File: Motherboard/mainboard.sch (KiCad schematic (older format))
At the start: 53 parts, among them IC1 BMX160, J1 Conn_01x01, J2 10118194-0001LF, J28 Conn_01x01, J29 Conn_01x01, J3 Micro_SD_Card, J30 Conn_01x01, J4 xf2m-2415-1a, J5 XF2M-1015-1A, J6 U.FL-R-SMT-1, J7 U.FL-R-SMT-1, J8 Conn_01x01, SW1 KMR231NG LFS, U1 RFM95W-915S2, U2 ATSAMD51G_TQFN48, U3 DRV8848, U4 TPS82740BSIPR, U5 DRV8848, U6 MAX708RESA-T, U8 RFM95W-915S2

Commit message: lots of clean up
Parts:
- removed D1: GREEN, LED_SMD:LED_0603_1608Metric, symbol mainboard-rescue:LED0805_NOOUTLINE-
- removed R1: 330, Resistor_SMD:R_0402_1005Metric, symbol mainboard-rescue:R_US-Device
- added D3: WS2812B, LED_SMD:LED_WS2812B_PLCC4_5.0x5.0mm_P3.2mm, symbol LED:WS2812B
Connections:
- net labels removed: CS_IMU
- wire segments 148 -> 147
- no-connect marks 10 -> 11
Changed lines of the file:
@@
-$EndComp
-$Comp
-L mainboard-rescue:R_US-Device R1
-U 1 1 5C3B885A
-P -250 6000
-F 0 "R1" H -350 5950 50  0000 C CNN
-F 1 "330" H -400 6050 50  0000 C CNN
-F 2 "Resistor_SMD:R_0402_1005Metric" V -210 5990 50  0001 C CNN
-F 3 "~" H -250 6000 50  0001 C CNN
-	1    -250 6000
-	-1   0    0    1
-$EndComp
-$Comp
-L mainboard-rescue:LED0805_NOOUTLINE- D?
-U 1 1 5C3B8860
-P -450 6150
-AR Path="/5BCFDB7D/5C3B8860" Ref="D?"  Part="1"
-AR Path="/5C3B8860" Ref="D1"  Part="1"
-F 0 "D1" H -500 6050 42  0000 C CNN
-F 1 "GREEN" H -600 6350 42  0001 C CNN
-F 2 "LED_SMD:LED_0603_1608Metric" H -450 6150 50  0001 C CNN
-F 3 "" H -450 6150 50  0001 C CNN
-	1    -450 6150
-	-1   0    0    1
 $EndComp
 $Comp
@@
 L power:GND #PWR0121
 U 1 1 5DB132FE
-P -600 6150
-F 0 "#PWR0121" H -600 5900 50  0001 C CNN
-F 1 "GND" H -595 5977 50  0000 C CNN
-F 2 "" H -600 6150 50  0001 C CNN
-F 3 "" H -600 6150 50  0001 C CNN
-	1    -600 6150
-	1    0    0    -1
-$EndComp
-Wire Wire Line
-	-600 6150 -550 6150
+P 650 6300
+F 0 "#PWR0121" H 650 6050 50  0001 C CNN
+F 1 "GND" H 655 6127 50  0000 C CNN
+F 2 "" H 650 6300 50  0001 C CNN
+F 3 "" H 650 6300 50  0001 C CNN
+	1    650  6300
+	1    0    0    -1
+$EndComp
 $Comp
 L power:GND #PWR0122
@@
 	1    0    0    -1
 $EndComp
-Text GLabel 2600 1600 2    59   Output ~ 0
-MOSI
-Text GLabel 2600 1500 2    59   Output ~ 0
-SCK
-Wire Wire Line
-	2600 1600 2500 1600
-Wire Wire Line
-	2600 1500 2500 1500
-Text GLabel 1200 1000 0    59   Input ~ 0
-MISO
-Wire Wire Line
-	1200 1000 1300 1000
-Wire Wire Line
-	2500 1400 2600 1400
-Text GLabel 2600 1400 2    50   Input ~ 0
-CS_IMU
 $Comp
 L power:GND #PWR0104
@@
 L power:+3V3 #PWR0105
 U 1 1 5DB0AC45
-P 2500 850
-F 0 "#PWR0105" H 2500 700 50  0001 C CNN
-F 1 "+3V3" H 2515 1023 50  0000 C CNN
-F 2 "" H 2500 850 50  0001 C CNN
-F 3 "" H 2500 850 50  0001 C CNN
-	1    2500 850
-	1    0    0    -1
-$EndComp
-Wire Wire Line
-	2500 850  2500 1000
+P 2600 850
+F 0 "#PWR0105" H 2600 700 50  0001 C CNN
+F 1 "+3V3" H 2615 1023 50  0000 C CNN
+F 2 "" H 2600 850 50  0001 C CNN
+F 3 "" H 2600 850 50  0001 C CNN
+	1    2600 850
+	1    0    0    -1
+$EndComp
+Wire Wire Line
+	2600 850  2600 1000
 $Comp
 L power:+3V3 #PWR0106
@@
 $EndComp
 Wire Wire Line
-	2700 1000 2500 1000
-Connection ~ 2500 1000
+	2700 1000 2600 1000
 $Comp
 L power:GND #PWR02
@@
 Wire Wire Line
 	8950 5750 8850 5750
-Text GLabel -1100 4850 2    50   Output ~ 0
-CS_IMU
 $Comp
 L power:GND #PWR0129
@@
 	1    0    0    -1
 $EndComp
+Text GLabel 2500 1600 2    59   BiDi ~ 0
+SDA1
+Text GLabel 2500 1500 2    59   BiDi ~ 0
+SCL1
+Wire Wire Line
+	2500 1400 2600 1400
+Wire Wire Line
+	2600 1400 2600 1000
+Connection ~ 2600 1000
+Wire Wire Line
+	2600 1000 2500 1000
+NoConn ~ 1300 1000
+$Comp
+L LED:WS2812B D3
+U 1 1 5DD8FF29
+P 650 6000
+F 0 "D3" H 306 6046 50  0000 R CNN
+F 1 "WS2812B" H 850 6400 50  0000 R CNN
+F 2 "LED_SMD:LED_WS2812B_PLCC4_5.0x5.0mm_P3.2mm" H 700 5700 50  0001 L TNN
+F 3 "https://cdn-shop.adafruit.com/datasheets/WS2812B.pdf" H 750 5625 50  0001 L TNN
+	1    650  6000
+	-1   0    0    -1
+$EndComp
+Wire Wire Line
+	950  6000 1450 6000
+$Comp
+L power:+3V3 #PWR0138
+U 1 1 5DDA79DB
+P 650 5700
+F 0 "#PWR0138" H 650 5550 50  0001 C CNN
+F 1 "+3V3" H 665 5873 50  0000 C CNN
+F 2 "" H 650 5700 50  0001 C CNN
+F 3 "" H 650 5700 50  0001 C CNN
+	1    650  5700
+	1    0    0    -1
+$EndComp

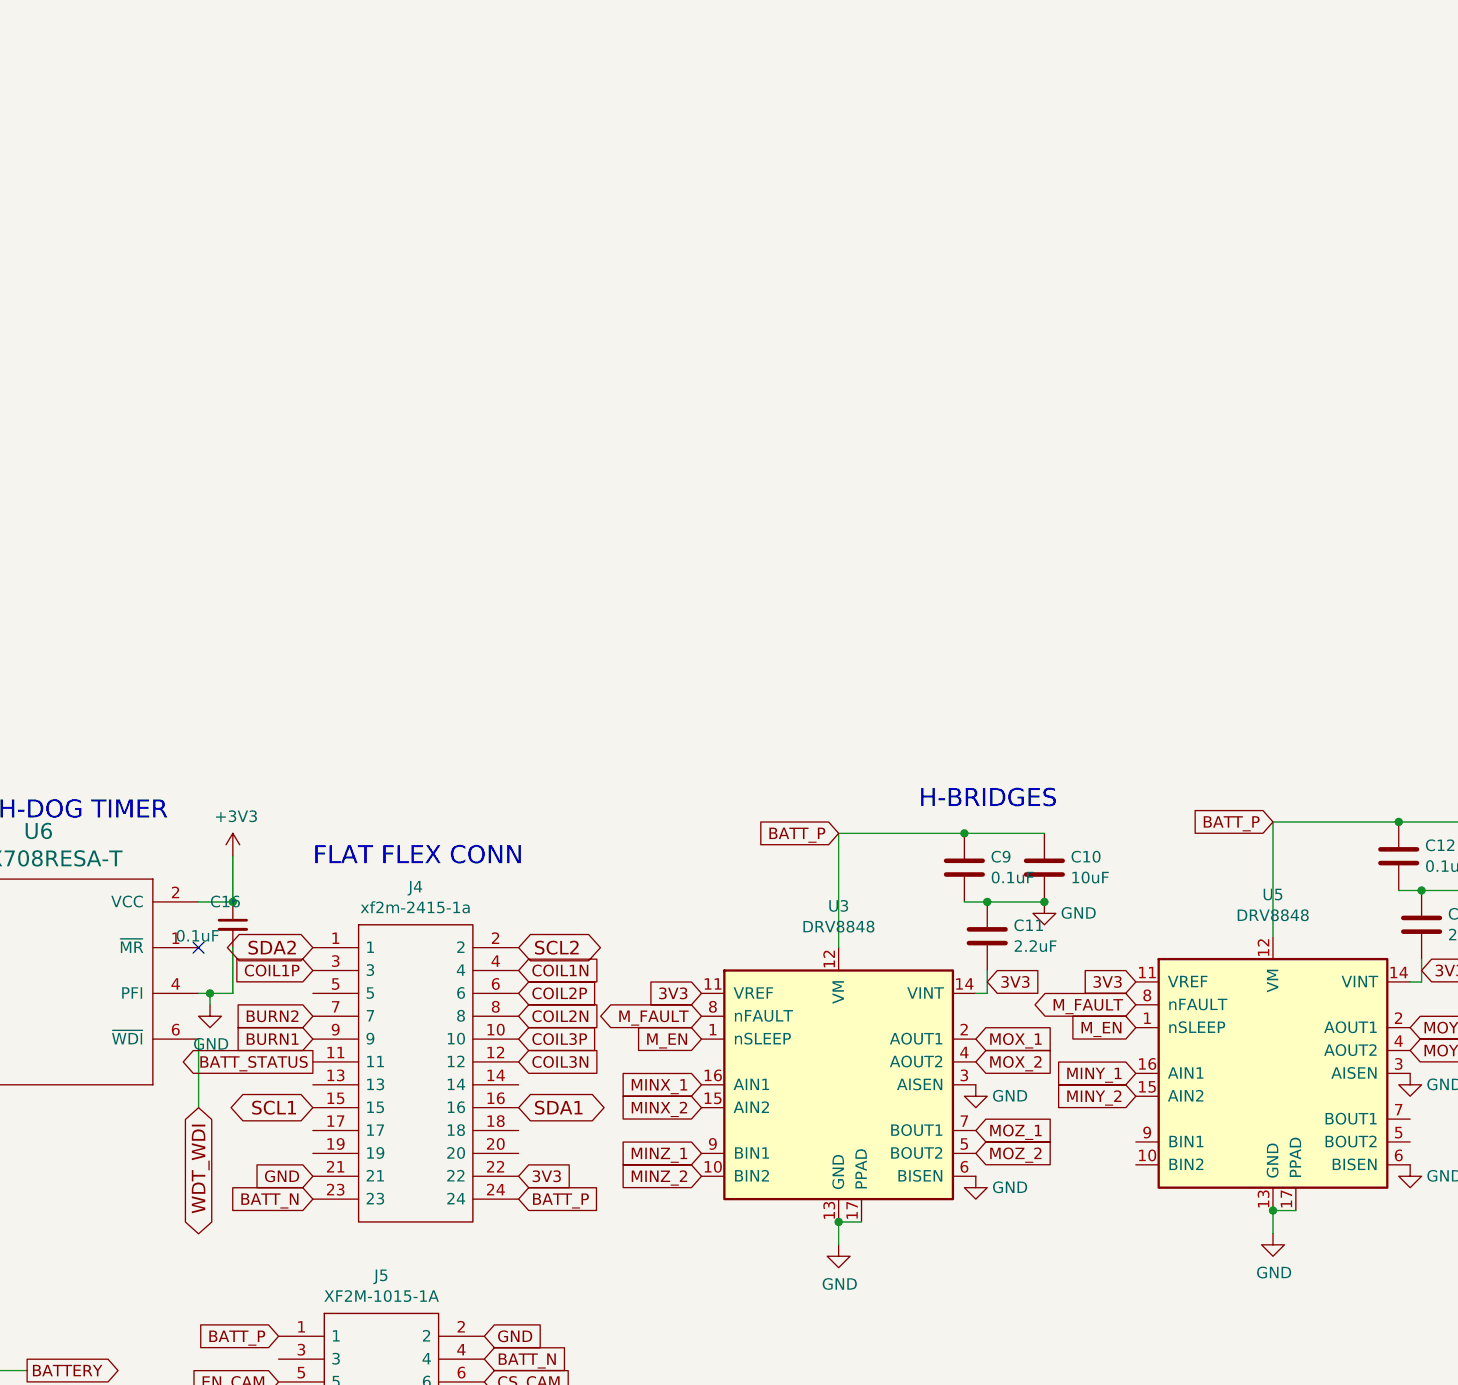
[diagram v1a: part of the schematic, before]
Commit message: putting matching coils in series
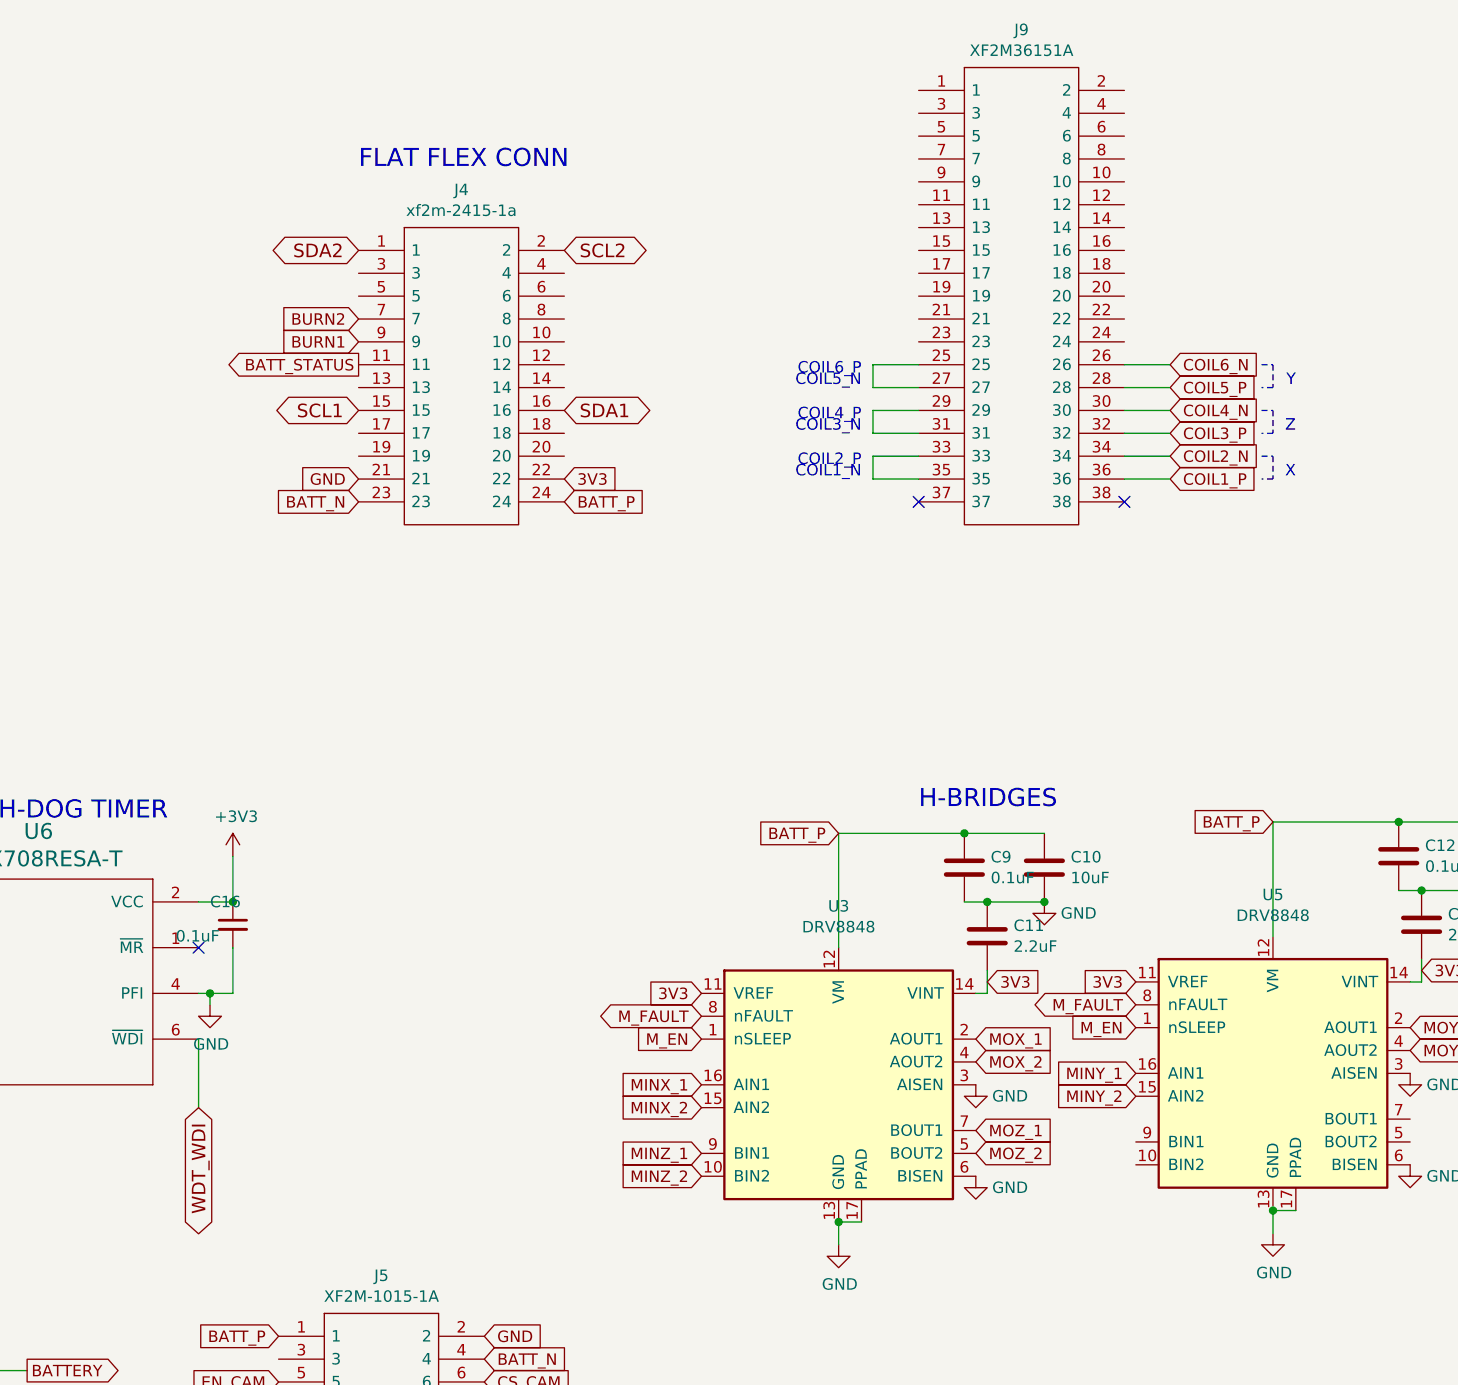
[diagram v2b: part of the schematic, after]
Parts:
- added J9: XF2M36151A, custom-footprints:XF2M36151A, symbol symbols:XF2M36151A
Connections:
- net COIL1N: no longer names the net of J4.4
- net COIL1P: no longer names the net of J4.3
- net COIL2N: no longer names the net of J4.8
- net COIL2P: no longer names the net of J4.6
- net COIL3N: no longer names the net of J4.12
- net COIL3P: no longer names the net of J4.10
- new net: J9.25, J9.27
- new net: J9.29, J9.31
- new net: J9.33, J9.35
- new net COIL1_P: J9.36
- new net COIL2_N: J9.34
- new net COIL3_P: J9.32
- new net COIL4_N: J9.30
- new net COIL5_P: J9.28
- new net COIL6_N: J9.26
- no-connect marks 11 -> 13
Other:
- note added: "COIL1_N"
- note added: "COIL2_P"
- note added: "COIL3_N"
- note added: "COIL4_P"
- note added: "COIL5_N"
- note added: "COIL6_P"
- note added: "X"
- note added: "Y"
- note added: "Z"
- moved on the sheet: J4
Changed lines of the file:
@@
 L mainboard-rescue:xf2m-2415-1a-symbols J4
 U 1 1 5DBA91E1
-P 5200 1250
-F 0 "J4" H 5650 1515 50  0000 C CNN
-F 1 "xf2m-2415-1a" H 5650 1424 50  0000 C CNN
-F 2 "custom-footprints:XF2M-2415-1A" H 5950 1350 50  0001 L CNN
-F 3 "http://docs-emea.rs-online.com/webdocs/0fd2/0900766b80fd28a0.pdf" H 5950 1250 50  0001 L CNN
-F 4 "Omron XF2M Series 0.5mm Pitch 24 Way 1 Row Right Angle SMT Female FPC Connector Locking Mechanism, Gold Plated Contacts" H 5950 1150 50  0001 L CNN "Description"
-	1    5200 1250
+P 5400 -1800
+F 0 "J4" H 5850 -1535 50  0000 C CNN
+F 1 "xf2m-2415-1a" H 5850 -1626 50  0000 C CNN
+F 2 "custom-footprints:XF2M-2415-1A" H 6150 -1700 50  0001 L CNN
+F 3 "http://docs-emea.rs-online.com/webdocs/0fd2/0900766b80fd28a0.pdf" H 6150 -1800 50  0001 L CNN
+F 4 "Omron XF2M Series 0.5mm Pitch 24 Way 1 Row Right Angle SMT Female FPC Connector Locking Mechanism, Gold Plated Contacts" H 6150 -1900 50  0001 L CNN "Description"
+	1    5400 -1800
 	1    0    0    -1
 $EndComp
@@
 Text Notes 1800 650  0    79   ~ 0
 IMU
-Text Notes 5200 900  0    79   ~ 0
+Text Notes 5400 -2150 0    79   ~ 0
 FLAT FLEX CONN
 $Comp
@@
 Text GLabel 5300 5800 2    59   BiDi ~ 0
 SCL2
-Text GLabel 6100 2250 2    50   Input ~ 0
+Text GLabel 6300 -800 2    50   Input ~ 0
 3V3
-Text GLabel 5200 2250 0    50   Input ~ 0
+Text GLabel 5400 -800 0    50   Input ~ 0
 GND
-Text GLabel 6100 2350 2    50   Input ~ 0
+Text GLabel 6300 -700 2    50   Input ~ 0
 BATT_P
-Text GLabel 5200 2350 0    50   Input ~ 0
+Text GLabel 5400 -700 0    50   Input ~ 0
 BATT_N
-Text GLabel 5200 1650 0    50   Input ~ 0
+Text GLabel 5400 -1400 0    50   Input ~ 0
 BURN1
-Text GLabel 5200 1550 0    50   Input ~ 0
+Text GLabel 5400 -1500 0    50   Input ~ 0
 BURN2
-Text GLabel 5200 1350 0    50   Input ~ 0
-COIL1P
-Text GLabel 6100 1350 2    50   Input ~ 0
-COIL1N
+Text GLabel 8950 -800 2    50   Input ~ 0
+COIL1_P
 Wire Wire Line
 	4750 1450 4700 1450
 Wire Wire Line
 	4750 1450 4750 1500
-Text GLabel 6100 1450 2    50   Input ~ 0
-COIL2P
-Text GLabel 6100 1550 2    50   Input ~ 0
-COIL2N
-Text GLabel 6100 1650 2    50   Input ~ 0
-COIL3P
-Text GLabel 6100 1750 2    50   Input ~ 0
-COIL3N
+Text GLabel 8950 -1000 2    50   Input ~ 0
+COIL3_P
 Text GLabel 5300 5900 2    59   BiDi ~ 0
 SDA2
@@
 Text Notes 2600 7900 0    50   ~ 0
 I2C_1\nSCL: PA01\nSDA: PA00\n\nI2C_2\nSCL: PA16\nSDA: PA17\n
-Text GLabel 6100 1950 2    59   BiDi ~ 0
+Text GLabel 6300 -1100 2    59   BiDi ~ 0
 SDA1
-Text GLabel 5200 1950 0    59   BiDi ~ 0
+Text GLabel 5400 -1100 0    59   BiDi ~ 0
 SCL1
-Text GLabel 6100 1250 2    59   BiDi ~ 0
+Text GLabel 6300 -1800 2    59   BiDi ~ 0
 SCL2
-Text GLabel 5200 1250 0    59   BiDi ~ 0
+Text GLabel 5400 -1800 0    59   BiDi ~ 0
 SDA2
 $Comp
@@
 Text GLabel 4450 6000 2    50   Input ~ 0
 BATT_STATUS
-Text GLabel 5200 1750 0    50   Output ~ 0
+Text GLabel 5400 -1300 0    50   Output ~ 0
 BATT_STATUS
 Text GLabel 4450 4700 2    50   BiDi ~ 0
@@
 	1    0    0    -1
 $EndComp
+$Comp
+L symbols:XF2M36151A J9
+U 1 1 5DB2822E
+P 7850 -2500
+F 0 "J9" H 8300 -2235 50  0000 C CNN
+F 1 "XF2M36151A" H 8300 -2326 50  0000 C CNN
+F 2 "custom-footprints:XF2M36151A" H 8600 -2400 50  0001 L CNN
+F 3 "http://static6.arrow.com/aropdfconversion/f8465b8f741f73dad8a8ab6be1baa1fc7c7bc980/19899915823643en-xf2m.pdf" H 8600 -2500 50  0001 L CNN
+F 4 "Rotary Backlock Connector (0.5-mm Pitch, Dual-sided Contact)" H 8600 -2600 50  0001 L CNN "Description"
+F 5 "3" H 8600 -2700 50  0001 L CNN "Height"
+F 6 "Omron Electronics" H 8600 -2800 50  0001 L CNN "Manufacturer_Name"
+F 7 "XF2M36151A" H 8600 -2900 50  0001 L CNN "Manufacturer_Part_Number"
+F 8 "" H 8600 -3000 50  0001 L CNN "Mouser Part Number"
+F 9 "" H 8600 -3100 50  0001 L CNN "Mouser Price/Stock"
+F 10 "" H 8600 -3200 50  0001 L CNN "RS Part Number"
+F 11 "" H 8600 -3300 50  0001 L CNN "RS Price/Stock"
+F 12 "70354816" H 8600 -3400 50  0001 L CNN "Allied_Number"
+F 13 "https://www.alliedelec.com/omron-electronic-components-xf2m36151a/70354816/" H 8600 -3500 50  0001 L CNN "Allied Price/Stock"
+	1    7850 -2500
+	1    0    0    -1
+$EndComp
+NoConn ~ 8750 -700
+NoConn ~ 7850 -700
+Text GLabel 8950 -1100 2    50   Input ~ 0
+COIL4_N
+Wire Wire Line
+	7850 -900 7650 -900
+Wire Wire Line
+	7650 -900 7650 -800
+Wire Wire Line
+	7650 -800 7850 -800
+Text Notes 7600 -800 2    50   ~ 0
+COIL1_N
+Wire Wire Line
+	7850 -1000 7650 -1000
+Wire Wire Line
+	7650 -1000 7650 -1100
+Wire Wire Line
+	7650 -1100 7850 -1100
+Text Notes 7600 -1000 2    50   ~ 0
+COIL3_N
+Text GLabel 8950 -1200 2    50   Input ~ 0
+COIL5_P
+Wire Wire Line
+	7850 -1300 7650 -1300
+Wire Wire Line
+	7650 -1300 7650 -1200
+Wire Wire Line
+	7650 -1200 7850 -1200
+Wire Wire Line
+	8750 -800 8950 -800
+Text GLabel 8950 -900 2    50   Input ~ 0
+COIL2_N
+Wire Wire Line
+	8950 -900 8750 -900
+Text Notes 7600 -850 2    50   ~ 0
+COIL2_P
+Text Notes 7600 -1050 2    50   ~ 0
+COIL4_P
+Text Notes 7600 -1200 2    50   ~ 0
+COIL5_N
+Text Notes 7600 -1250 2    50   ~ 0
+COIL6_P
+Wire Wire Line
+	8750 -1200 8950 -1200
+Wire Wire Line
+	8750 -1000 8950 -1000
+Wire Wire Line
+	8950 -1100 8750 -1100
+Text GLabel 8950 -1300 2    50   Input ~ 0
+COIL6_N
+Wire Wire Line
+	8950 -1300 8750 -1300
+Wire Notes Line
+	9350 -900 9400 -900
+Wire Notes Line
+	9400 -900 9400 -800
+Wire Notes Line
+	9400 -800 9350 -800
+Wire Notes Line
+	9350 -1100 9400 -1100
+Wire Notes Line
+	9400 -1100 9400 -1000
+Wire Notes Line
+	9400 -1000 9350 -1000
+Wire Notes Line
+	9350 -1300 9400 -1300
+Wire Notes Line
+	9400 -1300 9400 -1200
+Wire Notes Line
+	9400 -1200 9350 -1200
+Text Notes 9500 -1200 2    50   ~ 0
+Y
+Text Notes 9500 -1000 2    50   ~ 0
+Z
+Text Notes 9500 -800 2    50   ~ 0
+X
 $EndSCHEMATC
